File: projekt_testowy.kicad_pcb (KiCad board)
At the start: 2 copper layers, 4 parts

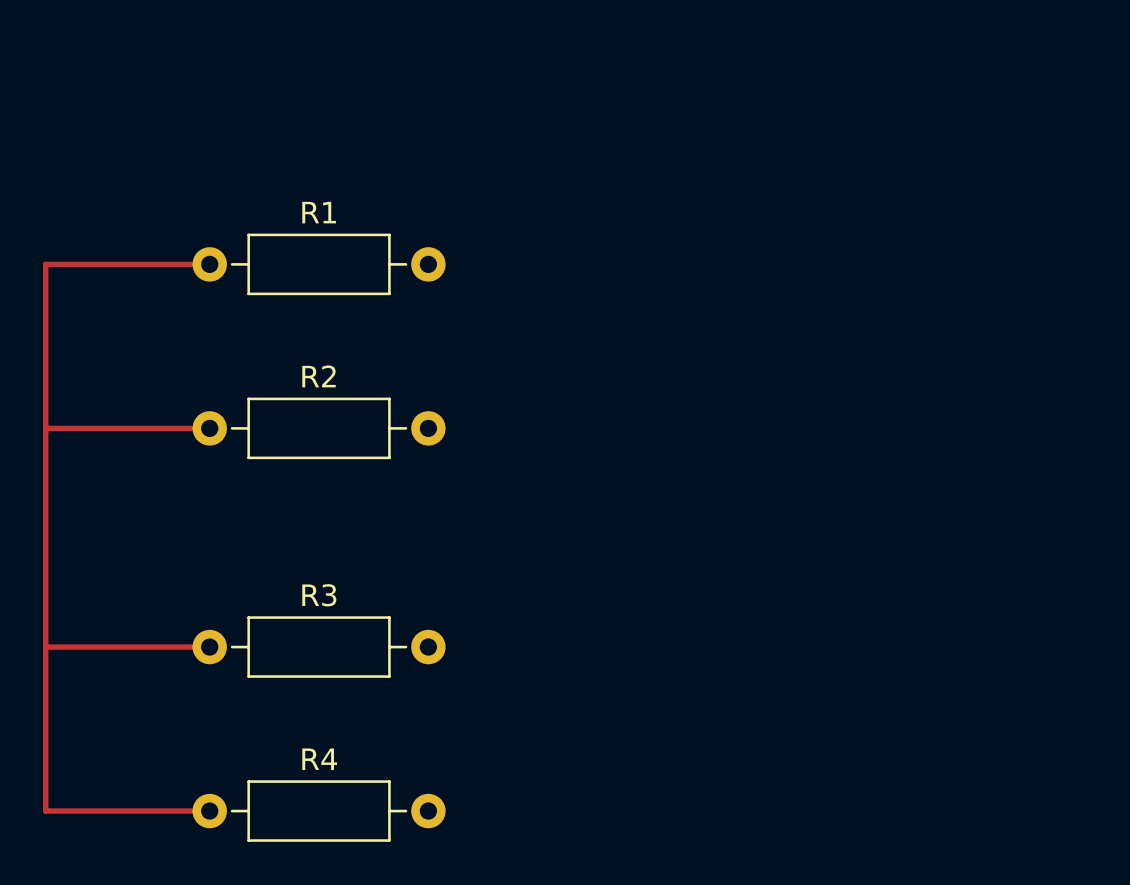
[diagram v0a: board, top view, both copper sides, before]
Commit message: dodanie krzywych polaczen
beda wymagac poprawy
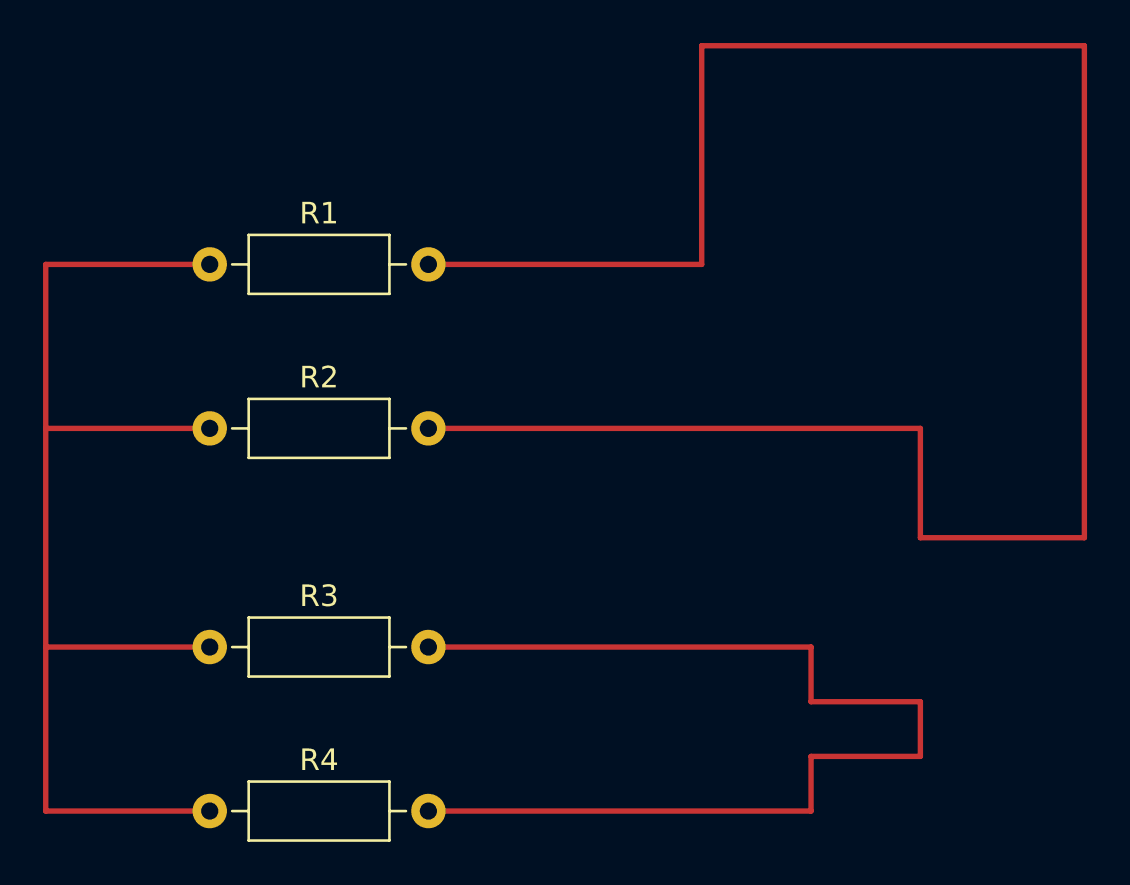
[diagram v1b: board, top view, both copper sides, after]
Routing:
- net GND: track 0.00 -> 152.4 mm
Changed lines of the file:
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@@
   (segment (start 81.28 60.96) (end 88.9 60.96) (width 0.25) (layer "F.Cu") (net 1))
   (segment (start 81.28 78.74) (end 88.9 78.74) (width 0.25) (layer "F.Cu") (net 1))
+  (segment (start 99.06 53.34) (end 111.76 53.34) (width 0.25) (layer "F.Cu") (net 2))
+  (segment (start 121.92 76.2) (end 116.84 76.2) (width 0.25) (layer "F.Cu") (net 2))
+  (segment (start 99.06 71.12) (end 116.84 71.12) (width 0.25) (layer "F.Cu") (net 2))
+  (segment (start 116.84 73.66) (end 121.92 73.66) (width 0.25) (layer "F.Cu") (net 2))
+  (segment (start 116.84 78.74) (end 99.06 78.74) (width 0.25) (layer "F.Cu") (net 2))
+  (segment (start 121.92 73.66) (end 121.92 76.2) (width 0.25) (layer "F.Cu") (net 2))
+  (segment (start 111.76 43.18) (end 129.54 43.18) (width 0.25) (layer "F.Cu") (net 2))
+  (segment (start 121.92 60.96) (end 99.06 60.96) (width 0.25) (layer "F.Cu") (net 2))
+  (segment (start 129.54 66.04) (end 121.92 66.04) (width 0.25) (layer "F.Cu") (net 2))
+  (segment (start 116.84 76.2) (end 116.84 78.74) (width 0.25) (layer "F.Cu") (net 2))
+  (segment (start 116.84 71.12) (end 116.84 73.66) (width 0.25) (layer "F.Cu") (net 2))
+  (segment (start 121.92 66.04) (end 121.92 60.96) (width 0.25) (layer "F.Cu") (net 2))
+  (segment (start 129.54 43.18) (end 129.54 66.04) (width 0.25) (layer "F.Cu") (net 2))
+  (segment (start 111.76 53.34) (end 111.76 43.18) (width 0.25) (layer "F.Cu") (net 2))
 )

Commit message: poprawa polaczen
polaczenia w linii
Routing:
- net GND: track 152.4 -> 25.4 mm
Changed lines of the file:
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@@
   (segment (start 81.28 60.96) (end 88.9 60.96) (width 0.25) (layer "F.Cu") (net 1))
   (segment (start 81.28 78.74) (end 88.9 78.74) (width 0.25) (layer "F.Cu") (net 1))
-  (segment (start 99.06 53.34) (end 111.76 53.34) (width 0.25) (layer "F.Cu") (net 2))
-  (segment (start 121.92 76.2) (end 116.84 76.2) (width 0.25) (layer "F.Cu") (net 2))
-  (segment (start 99.06 71.12) (end 116.84 71.12) (width 0.25) (layer "F.Cu") (net 2))
-  (segment (start 116.84 73.66) (end 121.92 73.66) (width 0.25) (layer "F.Cu") (net 2))
-  (segment (start 116.84 78.74) (end 99.06 78.74) (width 0.25) (layer "F.Cu") (net 2))
-  (segment (start 121.92 73.66) (end 121.92 76.2) (width 0.25) (layer "F.Cu") (net 2))
-  (segment (start 111.76 43.18) (end 129.54 43.18) (width 0.25) (layer "F.Cu") (net 2))
-  (segment (start 121.92 60.96) (end 99.06 60.96) (width 0.25) (layer "F.Cu") (net 2))
-  (segment (start 129.54 66.04) (end 121.92 66.04) (width 0.25) (layer "F.Cu") (net 2))
-  (segment (start 116.84 76.2) (end 116.84 78.74) (width 0.25) (layer "F.Cu") (net 2))
-  (segment (start 116.84 71.12) (end 116.84 73.66) (width 0.25) (layer "F.Cu") (net 2))
-  (segment (start 121.92 66.04) (end 121.92 60.96) (width 0.25) (layer "F.Cu") (net 2))
-  (segment (start 129.54 43.18) (end 129.54 66.04) (width 0.25) (layer "F.Cu") (net 2))
-  (segment (start 111.76 53.34) (end 111.76 43.18) (width 0.25) (layer "F.Cu") (net 2))
+  (segment (start 99.06 60.96) (end 99.06 78.74) (width 0.25) (layer "F.Cu") (net 2))
+  (segment (start 99.06 53.34) (end 99.06 60.96) (width 0.25) (layer "F.Cu") (net 2))
 )
